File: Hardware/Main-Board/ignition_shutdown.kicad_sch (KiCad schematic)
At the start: 14 parts, among them U4 RP2040

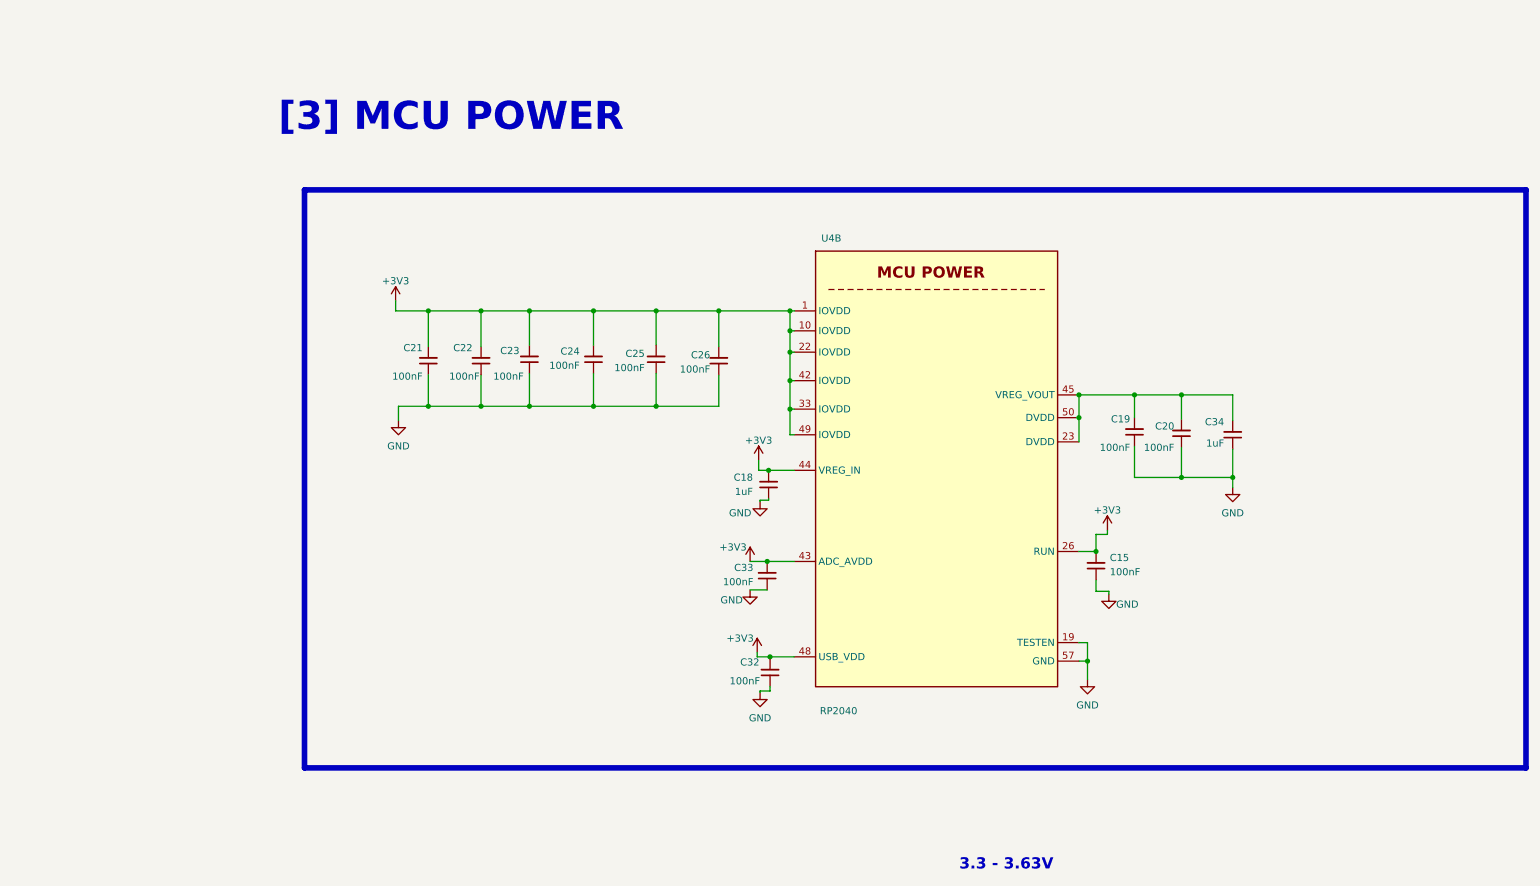
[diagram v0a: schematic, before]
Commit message: Done with main board design, and camera interconnect in progress
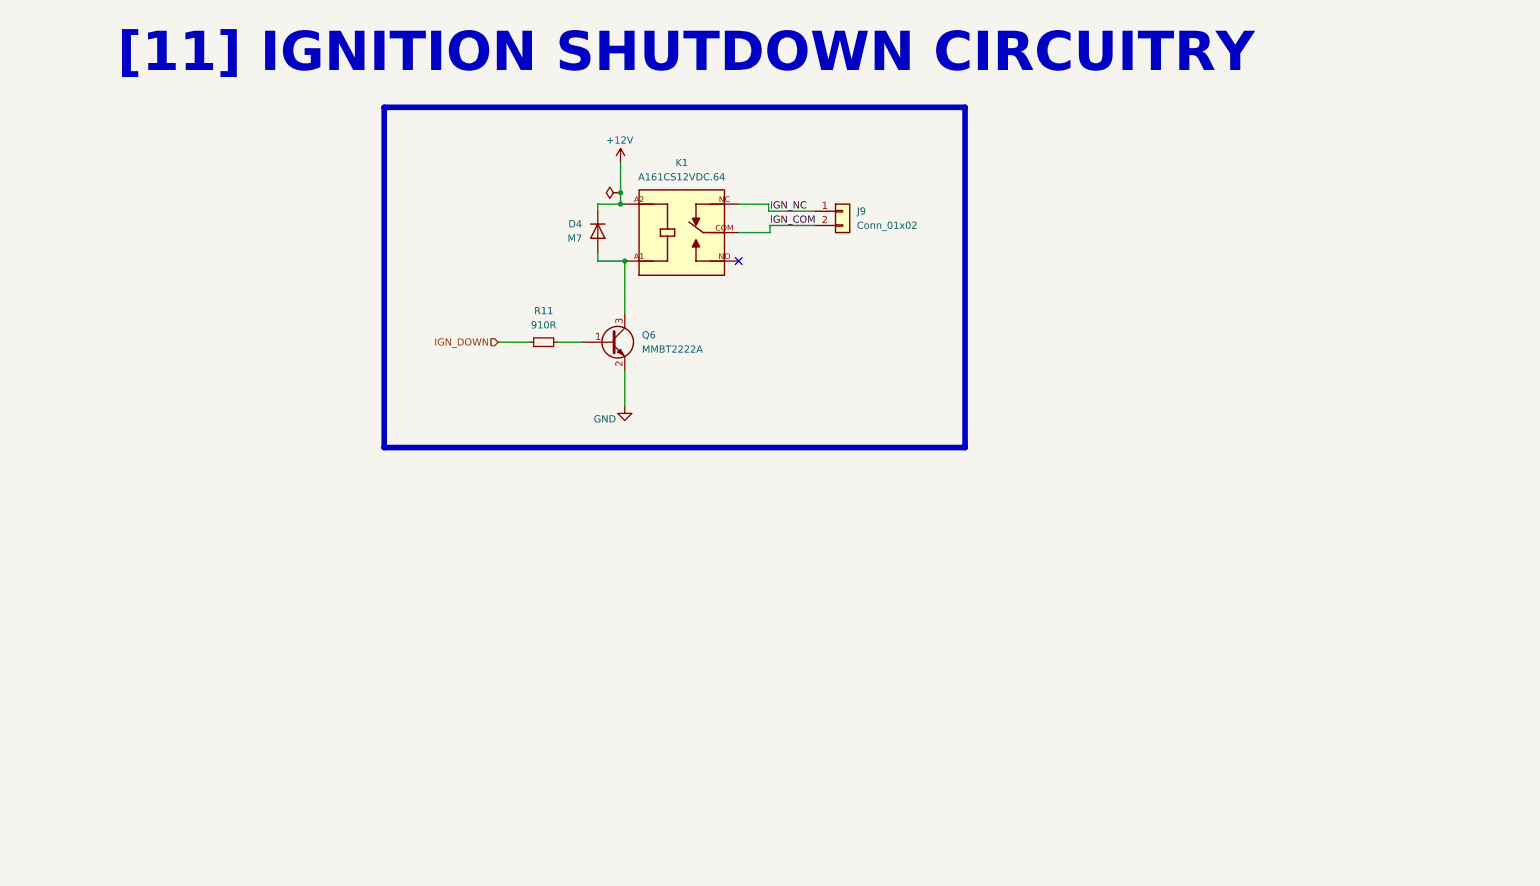
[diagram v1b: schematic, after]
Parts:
- removed C15, C19, C20, C21, C22, C23, C24, C25, C26, C32, C33: 100nF, Capacitor_SMD:C_0402_1005Metric, symbol Device:C_Small
- removed C18, C34: 1uF, Capacitor_SMD:C_0402_1005Metric, symbol Device:C_Small
- removed U4: RP2040, Package_DFN_QFN:QFN-56-1EP_7x7mm_P0.4mm_EP3.2x3.2mm, symbol MCU_RaspberryPi:RP2040
- added D4: M7, Diode_SMD:D_SMA, symbol Diode:1N4001
- added J9: Conn_01x02, Connector_TE-Connectivity:TE_440055-2_1x02_P2.00mm_Horizontal, symbol Connector_Generic:Conn_01x02
- added K1: A161CS12VDC.64, A161CS12VDC_64:RELAY_A161CS12VDC_64, symbol A161CS12VDC_64:A161CS12VDC.64
- added Q6: MMBT2222A, Package_TO_SOT_SMD:SOT-23, symbol Transistor_BJT:MMBT2222A
- added R11: 910R, Resistor_SMD:R_0402_1005Metric, symbol Device:R_Small
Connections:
- net GND: now also Q6.2 (E)
- new net: D4.2 (A), K1.A1, Q6.3 (C)
- new net: Q6.1 (B), R11.2
- new net +12V: D4.1 (K), K1.A2
- new net IGN_COM: J9.2 (Pin_2), K1.COM
- new net IGN_DOWN: R11.1
- new net IGN_NC: J9.1 (Pin_1), K1.NC
- no-connect marks 0 -> 1
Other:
- note added: "[11] IGNITION SHUTDOWN CIRCUITRY"
- note removed: "3.3 - 3.63V"
- note removed: "[3] MCU POWER"
